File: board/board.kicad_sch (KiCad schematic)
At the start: 5 parts, among them J1 001_I2C, J2 007_ADC, J3 001_I2C, J4 007_ADC

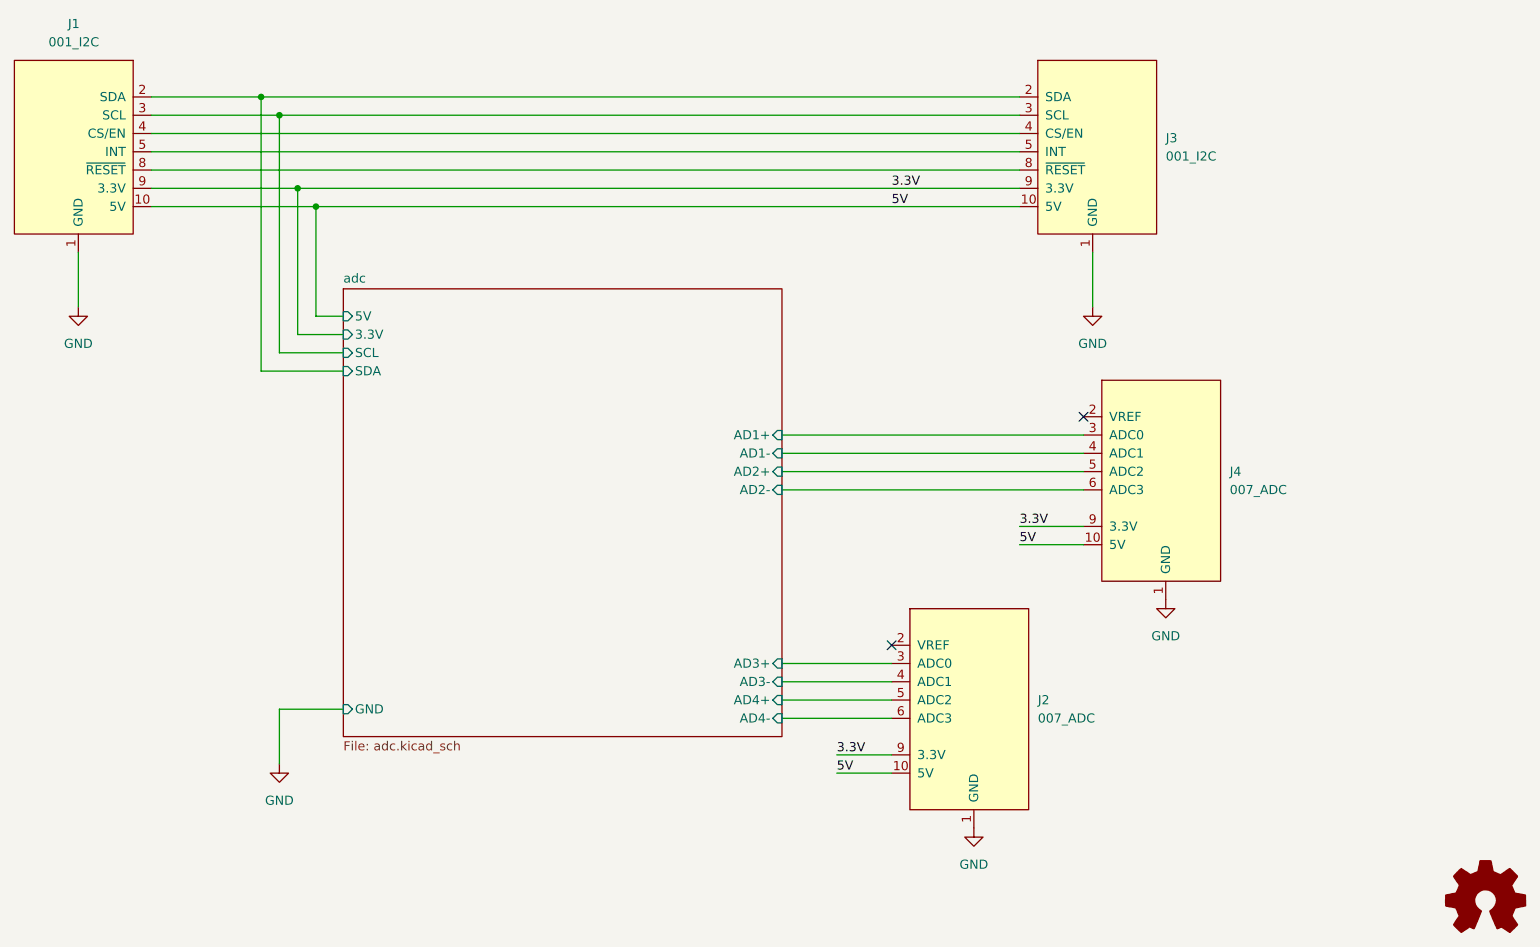
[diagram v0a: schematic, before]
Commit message: added copper pours and moved edgy specific components out of the subsheet
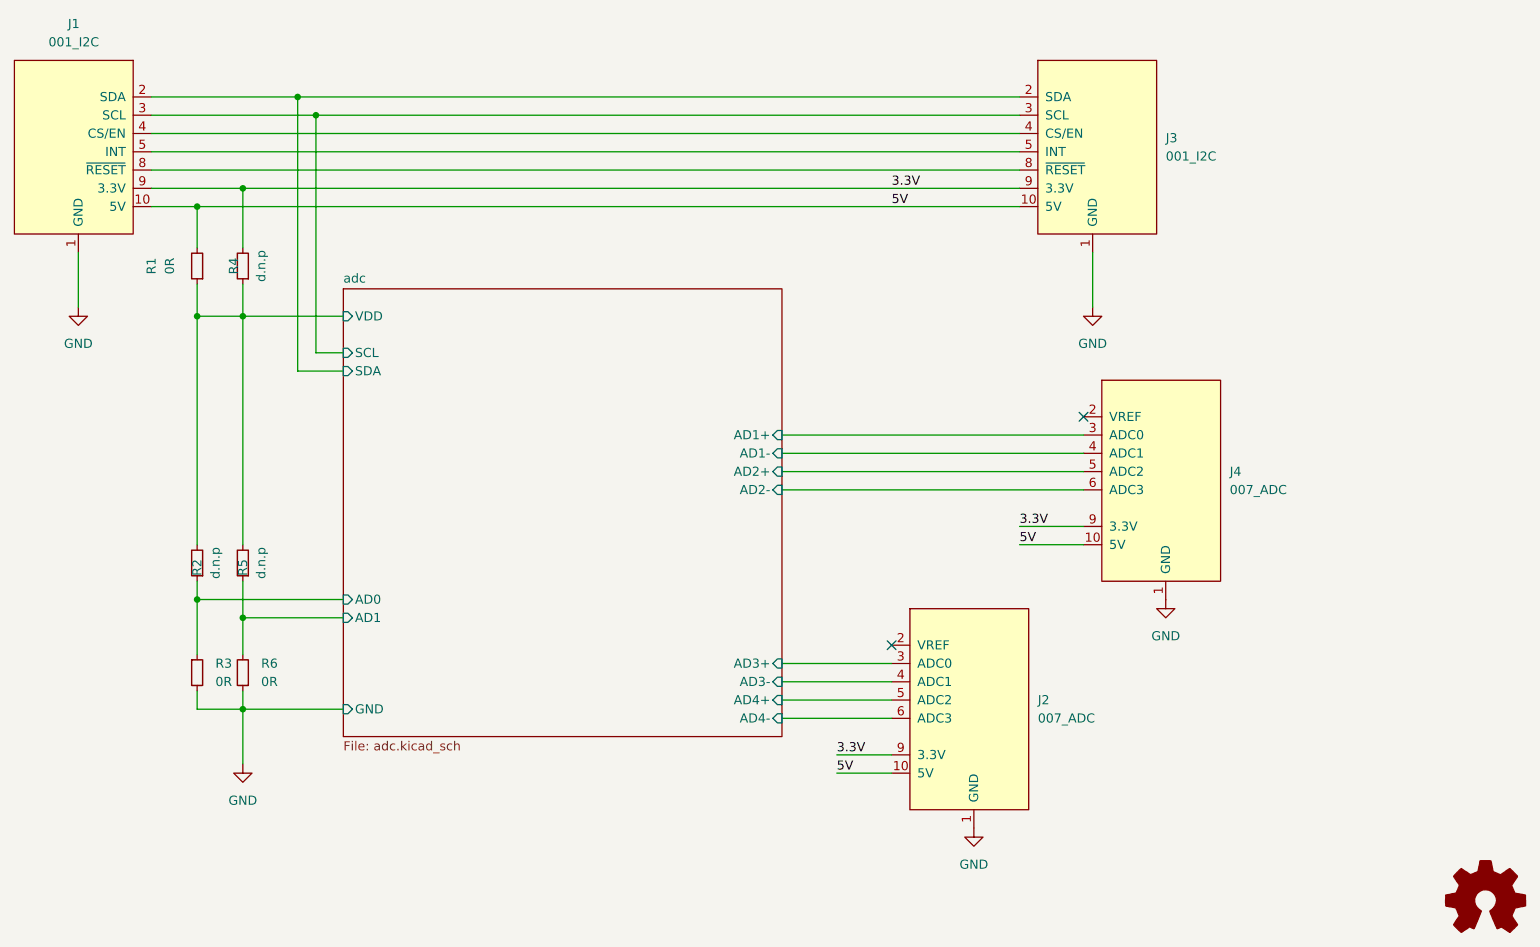
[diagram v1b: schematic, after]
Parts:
- added R1, R3, R6: 0R, Resistor_SMD:R_0603_1608Metric, symbol Device:R_Small
- added R2, R4, R5: d.n.p, Resistor_SMD:R_0603_1608Metric, symbol Device:R_Small
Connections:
- net 3.3V: now also R4.2
- net 5V: now also R1.2
- net GND: now also R3.2, R6.1
- new net adc/AD0: R2.1, R3.1
- new net adc/AD1: R5.1, R6.2
- new net adc/VDD: R1.1, R2.2, R4.1, R5.2
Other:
- sheet adc ports: added AD0, AD1, VDD; removed 3.3V, 5V
